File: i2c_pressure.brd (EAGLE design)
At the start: 100 x 80 mm, 4 parts, among them IC1 TCAN1051HGV, U1 SSCDANT030PASA5, U2 SSCDANT030PASA5, U3 SSCDANT030PASA5

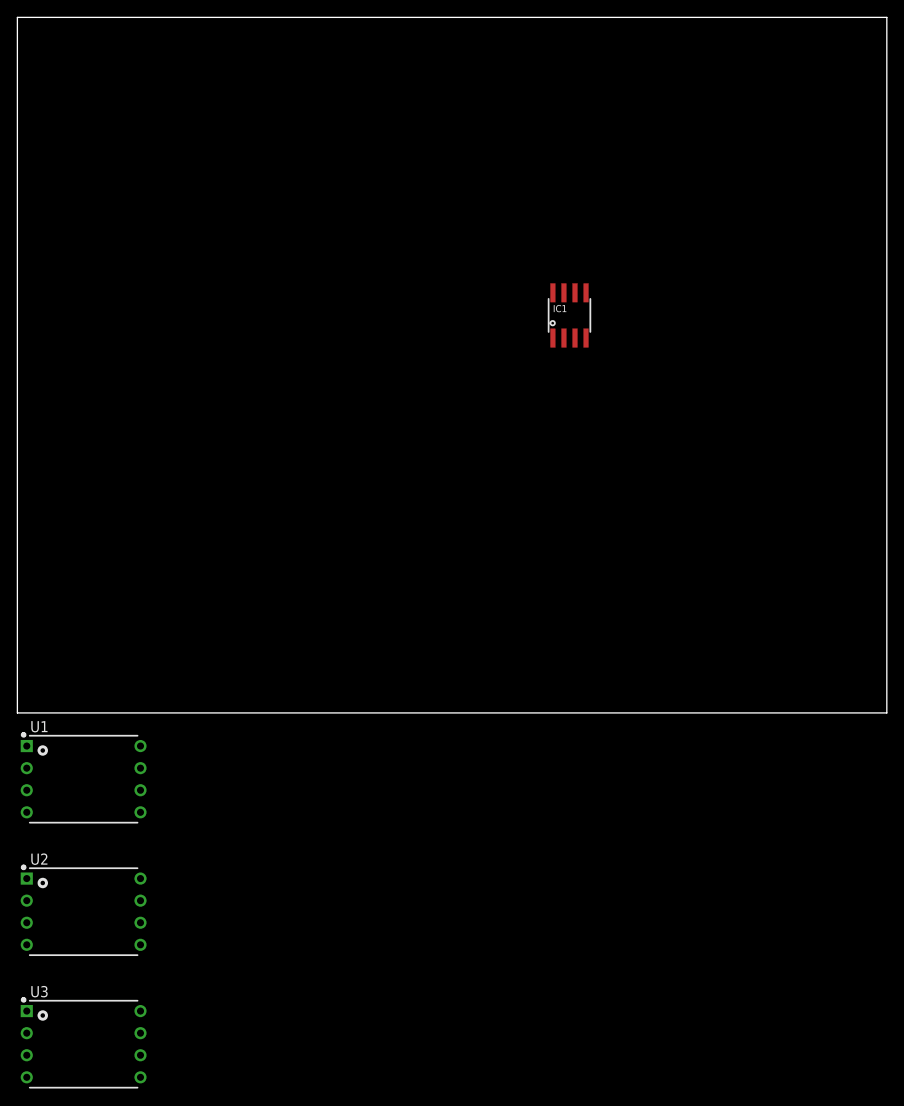
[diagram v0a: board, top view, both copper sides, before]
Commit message: pressure board needs i2c mux, introduce engmon-wroom
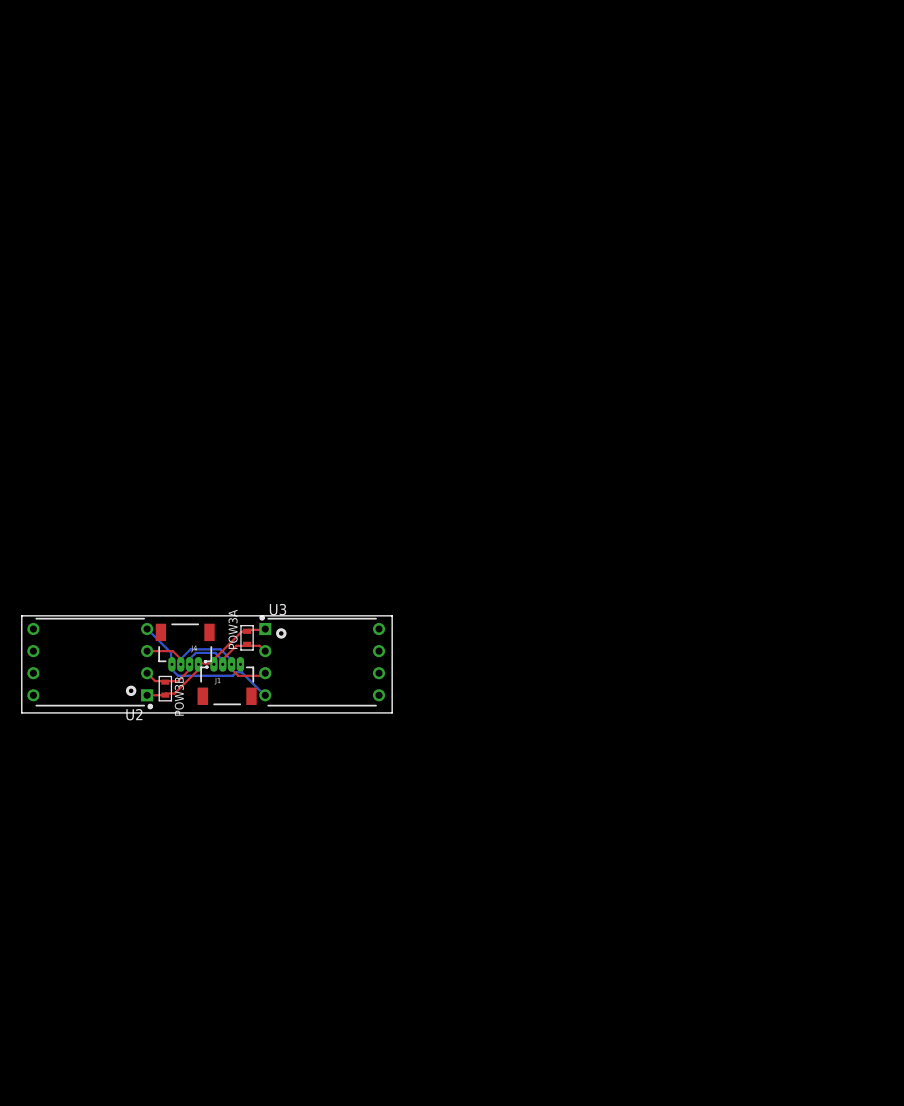
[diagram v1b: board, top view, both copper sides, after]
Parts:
- removed IC1: TCAN1051HGV, microbuilder:SOIC8_150MIL
- removed U1: SSCDANT030PASA5, SSCDANT030PASA5:XDCR_SSCDANT030PASA5
- added J1, J4: Vertical Qwiic Connector, 00jim:JST04_1MM_HOLES
- added POW3A, POW3B: (no value), MF_Passives:C0603
- moved U3 51.8 mm to (35.1, 5.84)
- moved U2 28.7 mm to (8.38, 5.84), turned to 180 degrees
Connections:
- removed net +5V: IC1.3
- removed net VCC_33: U2.2, U3.2
- removed net VIO: IC1.5
- removed net VSUP: U1.2
- new net VCC: J1.P$2, J4.P$2, POW3A.P$1, POW3B.P$1, U2.2, U3.2
- net GND: now also J1.P$1, J4.P$1, POW3A.P$2, POW3B.P$2; no longer IC1.2, U1.1
- net SCL: now also J1.P$4, J4.P$4
- net SDA: now also J1.P$3, J4.P$3
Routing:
- net SCL: track 0.00 -> 19.1 mm
- net VCC: track 0.00 -> 18.6 mm
- net GND: track 0.00 -> 17.8 mm
- net SDA: track 0.00 -> 17.7 mm
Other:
- board size 100 x 80 mm -> 42.6 x 11.2 mm

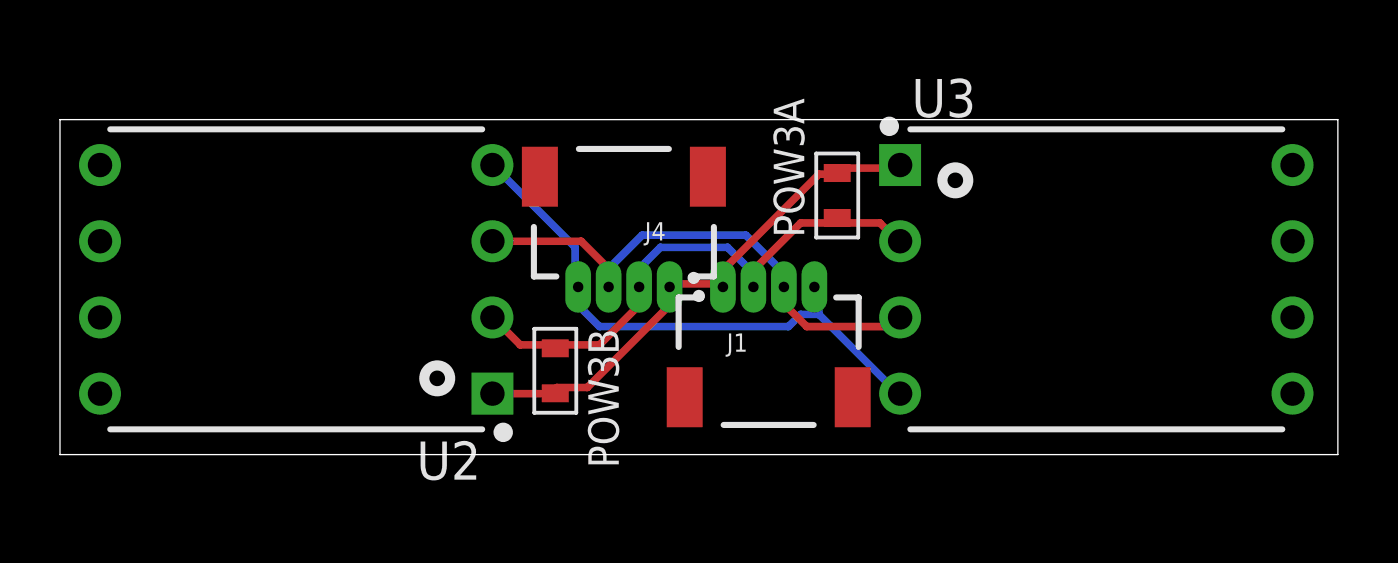
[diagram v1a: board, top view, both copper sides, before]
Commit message: add i2c multiplexer to 00jim and pressure board
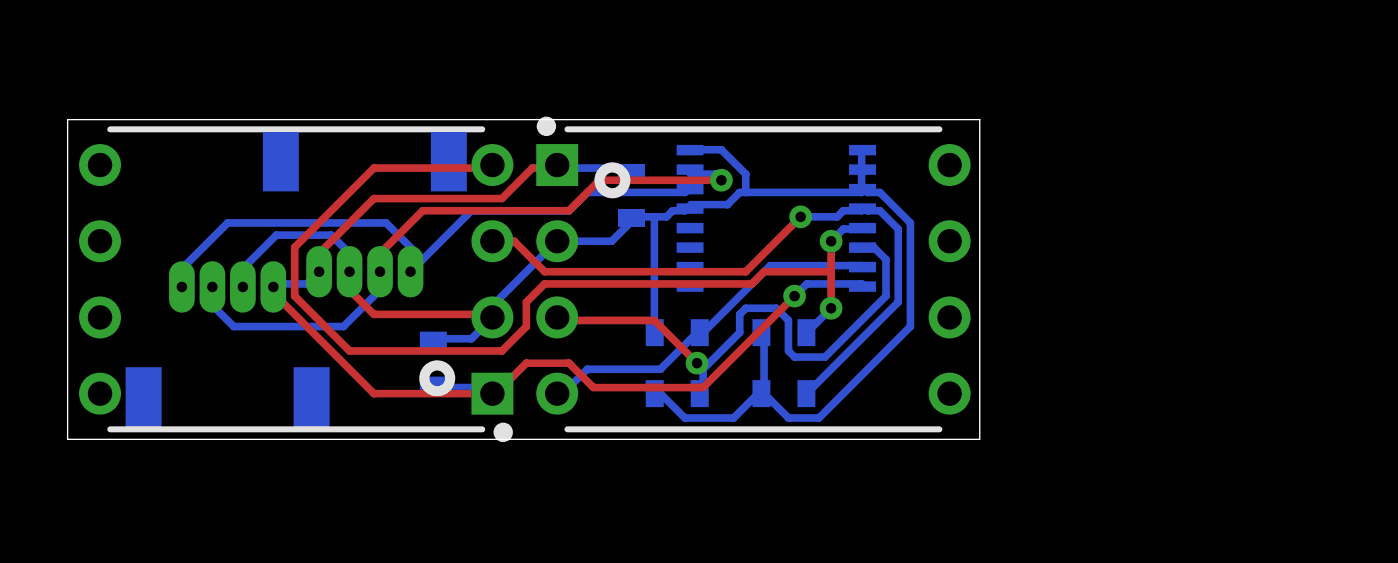
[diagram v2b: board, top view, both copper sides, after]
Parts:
- added RCAN, RCAN1, RCAN2, RCAN3: 2k7, 00jim:R0603
- added U$1: TCA9546ATSSOP16, analog-devices-3:TSSOP16
- POW3A, POW3B: value (none) -> 10uF
- moved J1 18.0 mm to (6.10, 1.78), flipped to the bottom
- moved U3 11.4 mm to (23.6, 5.84)
- moved J4 8.65 mm to (10.7, 9.91), flipped to the bottom
- moved POW3A 6.86 mm to (19.6, 8.64), flipped to the bottom
- moved POW3B 4.07 mm to (13.0, 3.05), flipped to the bottom
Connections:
- new net SC0: RCAN2.P$1, U$1.5, U2.4
- new net SC1: RCAN.P$1, U$1.7, U3.4
- new net SD0: RCAN3.P$1, U$1.4, U2.3
- new net SD1: RCAN1.P$1, U$1.6, U3.3
- net GND: now also U$1.8
- net SCL: now also U$1.14; no longer U2.4, U3.4
- net SDA: now also U$1.15; no longer U2.3, U3.3
- net VCC: now also RCAN.P$2, RCAN1.P$2, RCAN2.P$2, RCAN3.P$2, U$1.1, U$1.13, U$1.16, U$1.2, U$1.3
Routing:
- net VCC: track 18.6 -> 54.5 mm
- net SC0: track 0.00 -> 34.2 mm, vias 0 -> 2
- net GND: track 17.8 -> 39.7 mm, vias 0 -> 1
- net SD0: track 0.00 -> 21.9 mm, vias 0 -> 1
- net SD1: track 0.00 -> 18.1 mm, vias 0 -> 1
- net SC1: track 0.00 -> 12.0 mm
- net SDA: track 17.7 -> 21.9 mm, vias 0 -> 1
- net SCL: track 19.1 -> 20.2 mm
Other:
- board size 42.6 x 11.2 mm -> 30.4 x 10.7 mm
